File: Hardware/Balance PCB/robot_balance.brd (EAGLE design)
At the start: 100 x 50 mm, 54 parts, among them P1 10118194-0001LF, Q1 16Mhz

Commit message: Board layout
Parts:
- added B1, B2: (no value), SparkFun-Electromechanical:TACTILE-SWITCH-SMD
- added C5, C6: 0.1uF, SparkFun-Capacitors:0805
- renumbered JP3 to CONTROL, JP4 to MPU-9250
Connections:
- new net BUTTON1: B1.1, B1.2, C5.1, U$4.26
- new net BUTTON2: B2.1, B2.2, C6.1, U$4.27
- net GND: now also B1.3, B1.4, B2.3, B2.4, C5.2, C6.2
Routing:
- net BUTTON1: track 0.00 -> 67.7 mm, vias 0 -> 2
- net BUTTON2: track 0.00 -> 54.0 mm, vias 0 -> 2
- net SWO: track 51.3 -> 28.8 mm, vias 0 -> 2
- net !S1_ENABLE: track 102.2 -> 80.4 mm, vias 2 -> 1
- net S1_STEP: track 89.8 -> 69.6 mm, vias 2 -> 3
- net 5V: track 125.4 -> 141.0 mm, vias 1 -> 2
- net SWDIO: track 33.0 -> 48.5 mm, vias 2 -> 0
- net 3.3V: track 127.0 -> 142.3 mm, vias 9 -> 8
- net !S1_FAULT: track 67.4 -> 53.2 mm, vias 1 -> 3
- net S2_DIR: track 62.5 -> 49.3 mm
- net !S2_FAULT: track 55.0 -> 66.2 mm, vias 3 -> 2
- net S2_M1: track 25.1 -> 14.5 mm, vias 0 -> 1
- net S1_M1: track 87.9 -> 98.3 mm
- net SWCLK: track 25.3 -> 35.4 mm, vias 4 -> 0
- net S1_DIR: track 84.1 -> 75.5 mm, vias 2 -> 1
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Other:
- board text added: "ELEC3907 GROUP FOXTROT WINTER 2016"
- board text added: "MPU-9250"
- board text removed: "ELEC3907 GROUP FOXTROT 2016"

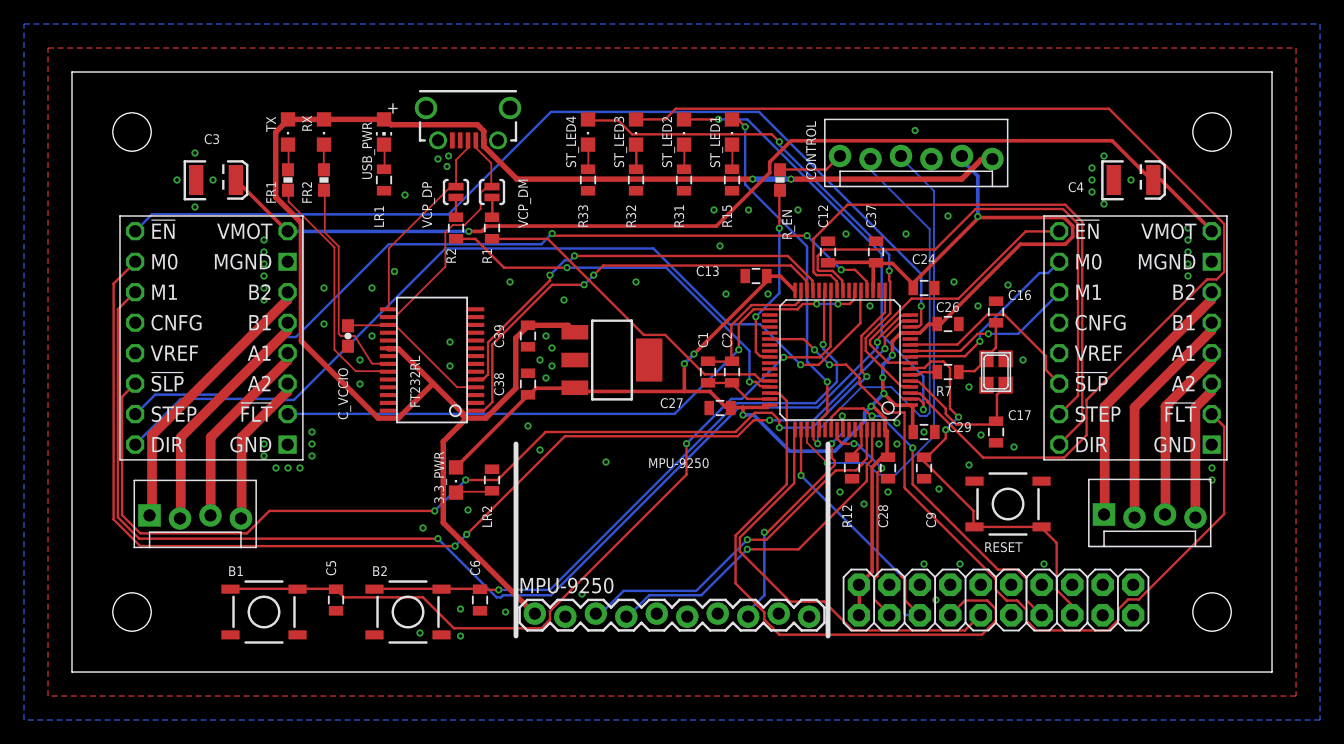
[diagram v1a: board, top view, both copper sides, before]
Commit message: Merged stepper and MPU projects
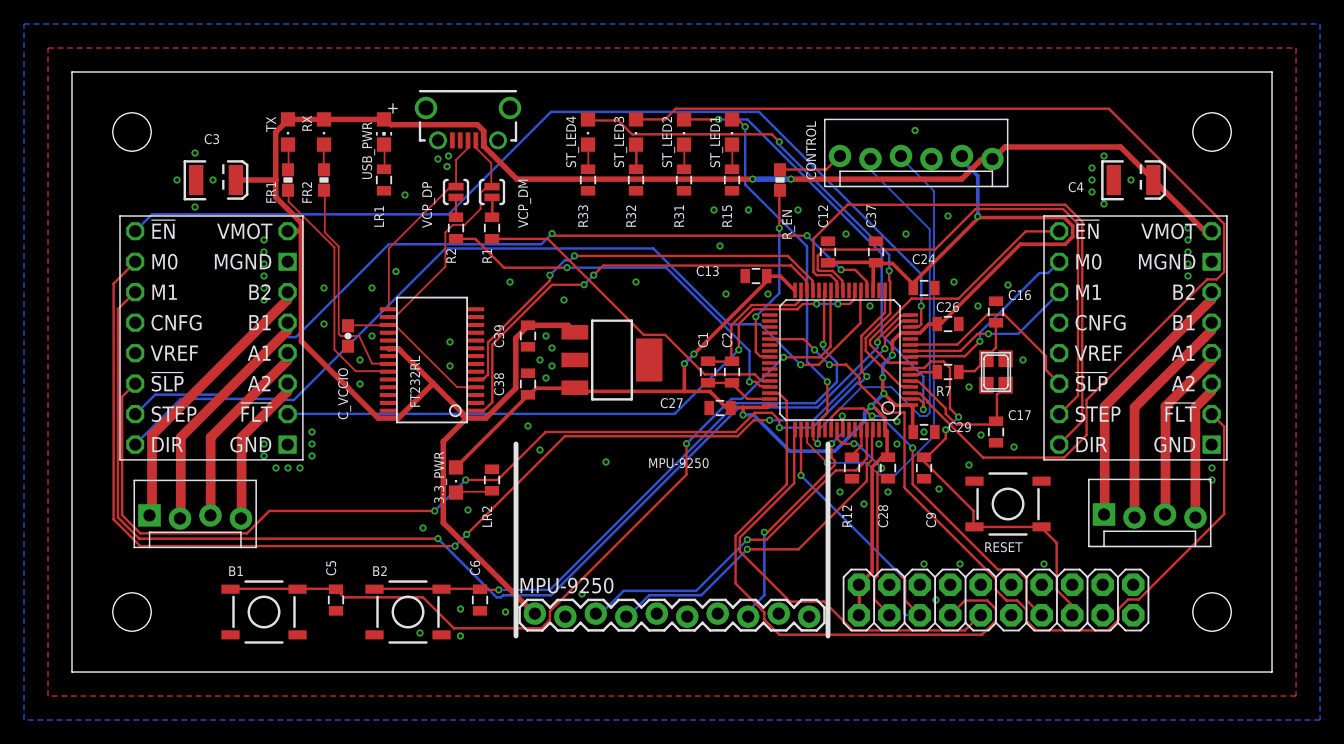
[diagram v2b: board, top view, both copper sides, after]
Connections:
- removed net V_USB: C3.A, C4.A, U$1.16, U$3.16
- net 5V: now also C3.A, C4.A, U$1.16, U$3.16
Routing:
- net V_USB: track 89.9 -> 0.00 mm, vias 1 -> 0
- net 5V: track 141.0 -> 167.1 mm
